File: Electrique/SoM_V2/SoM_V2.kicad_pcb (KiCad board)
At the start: 4 copper layers, 30 x 42.1 mm, 53 parts, among them Q501 MBT3904DW1T1G, U301 TCA9546APWR, U302 FT231XQ, U305 SN65HVD230, U401 PCA9633DP1, U501 ESP32-S3-MINI-1U

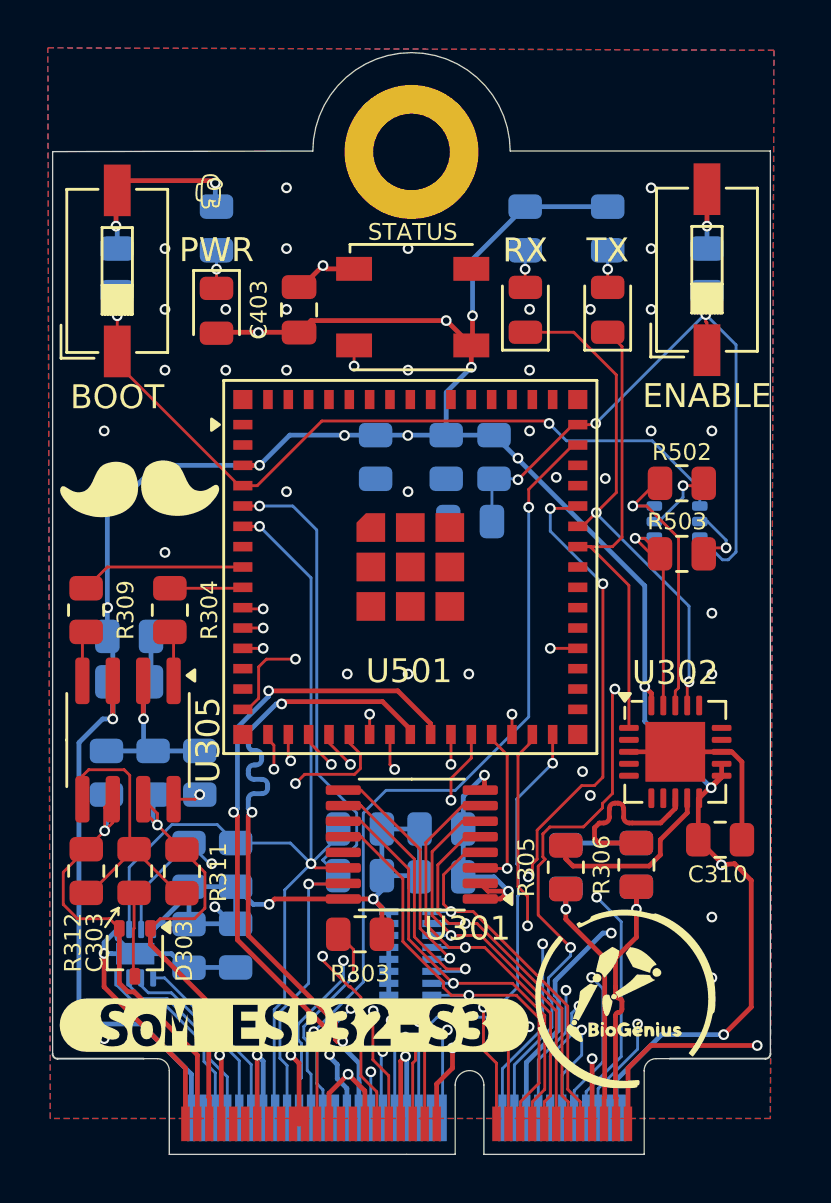
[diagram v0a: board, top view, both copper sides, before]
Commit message: Some modif of traces
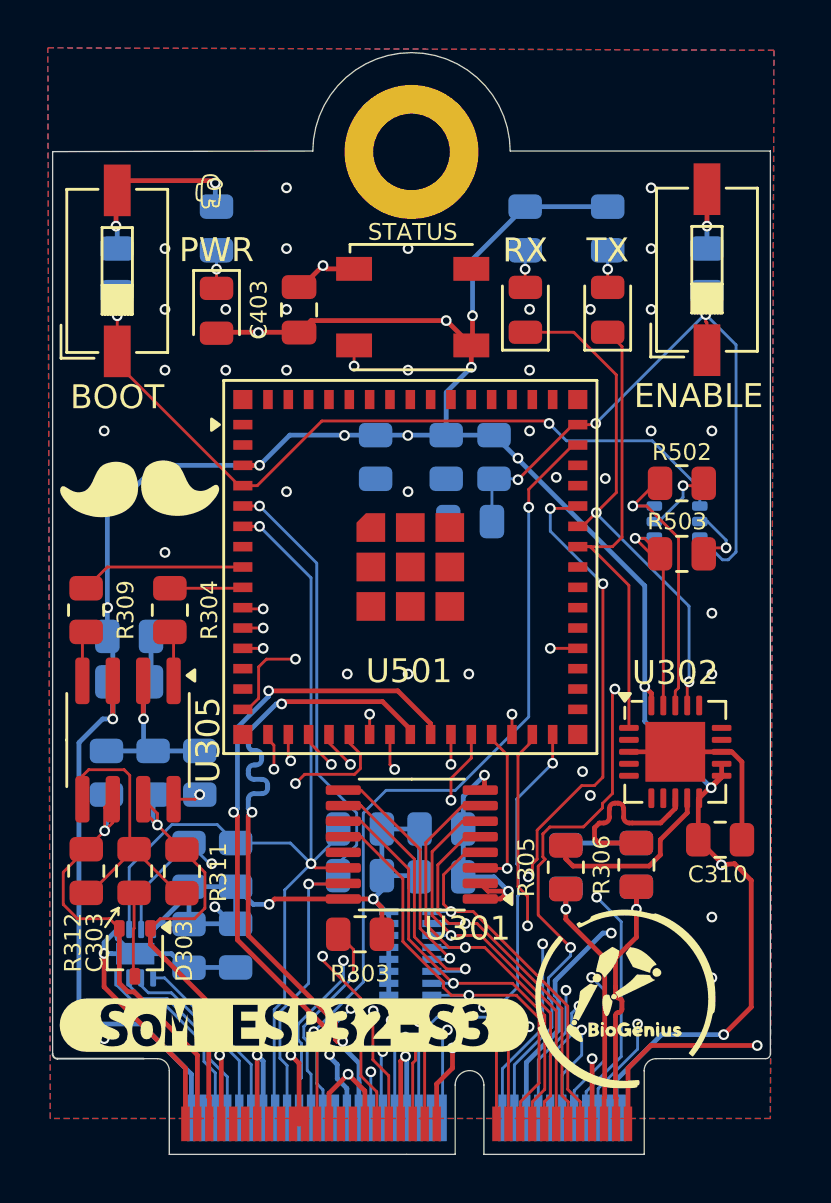
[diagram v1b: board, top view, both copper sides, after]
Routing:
- net I2C_SDA_ESP32: track 43.4 -> 41.5 mm
- net CHIP_EN: track 66.6 -> 65.7 mm
- net GPIO34: track 21.9 -> 21.1 mm
- net I2S_DIN/DOUT: track 25.2 -> 24.7 mm
